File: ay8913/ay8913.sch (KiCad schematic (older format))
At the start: 5 parts, among them U2 74HCT138, U3 GAL16V8, U4 AY-3-8913, U5 XTAL_OSC_HALF_CAN, U6 74HC74

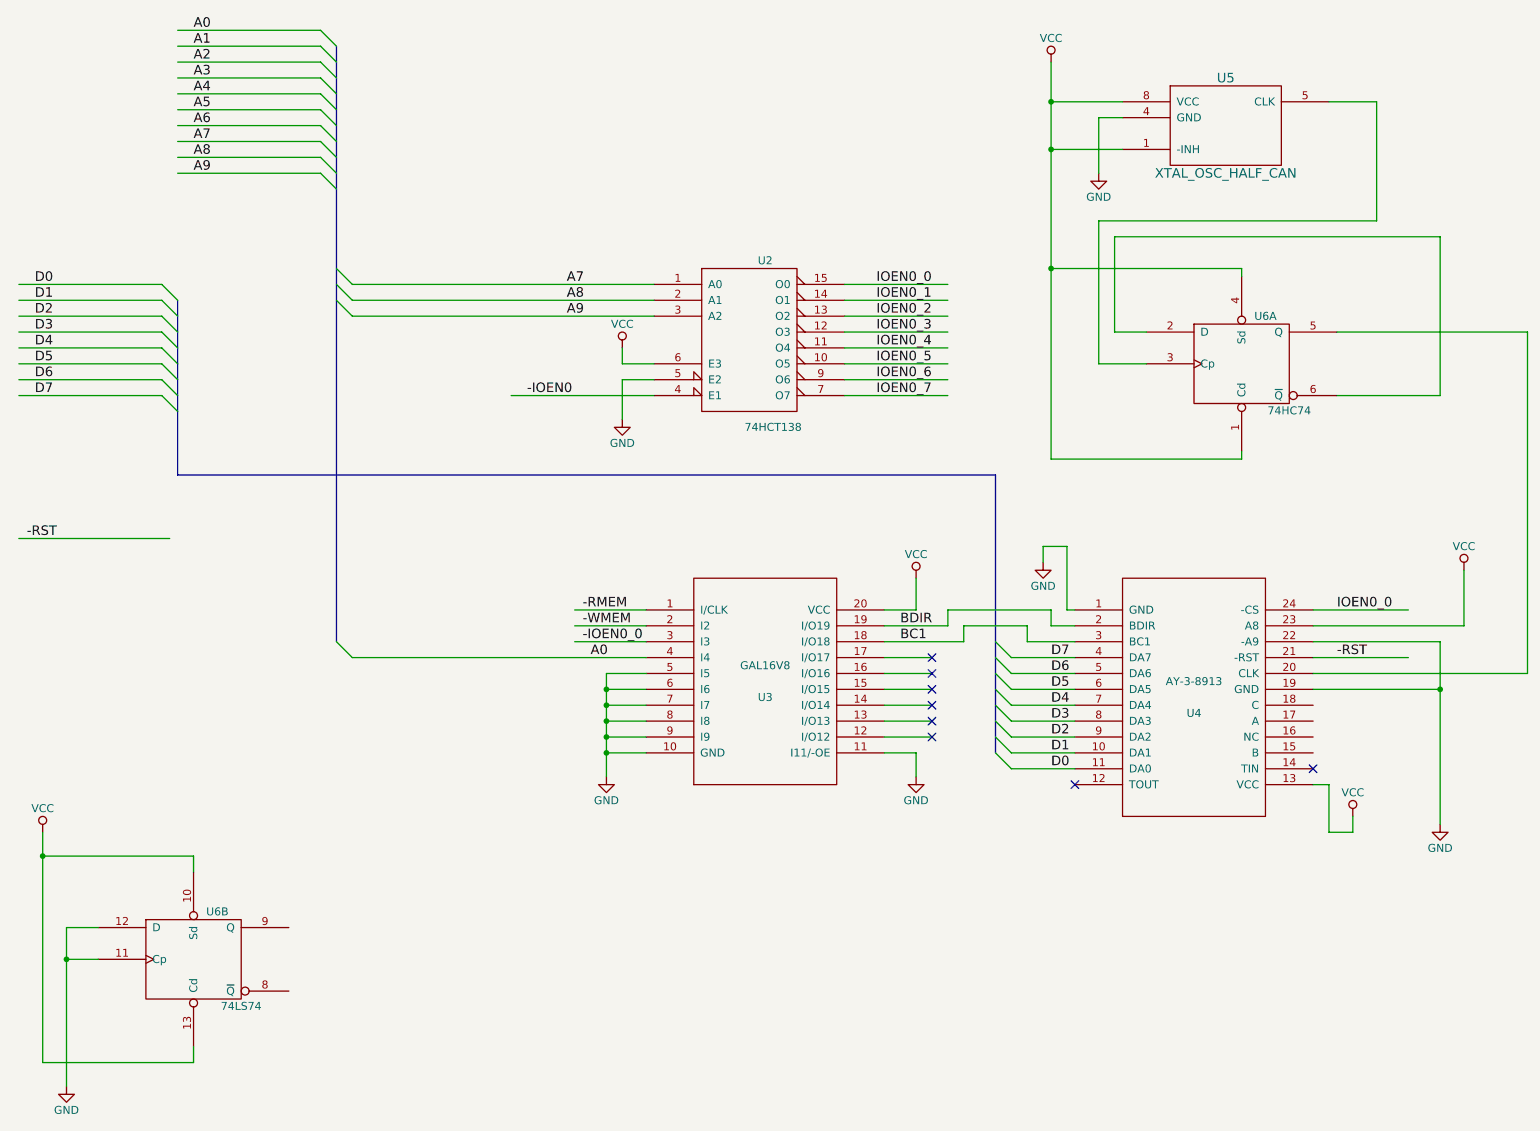
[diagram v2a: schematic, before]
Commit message: use GAL16V8 to divide the 4MHz to 2MHz
This works fine and eliminates the need for the 74HC74.
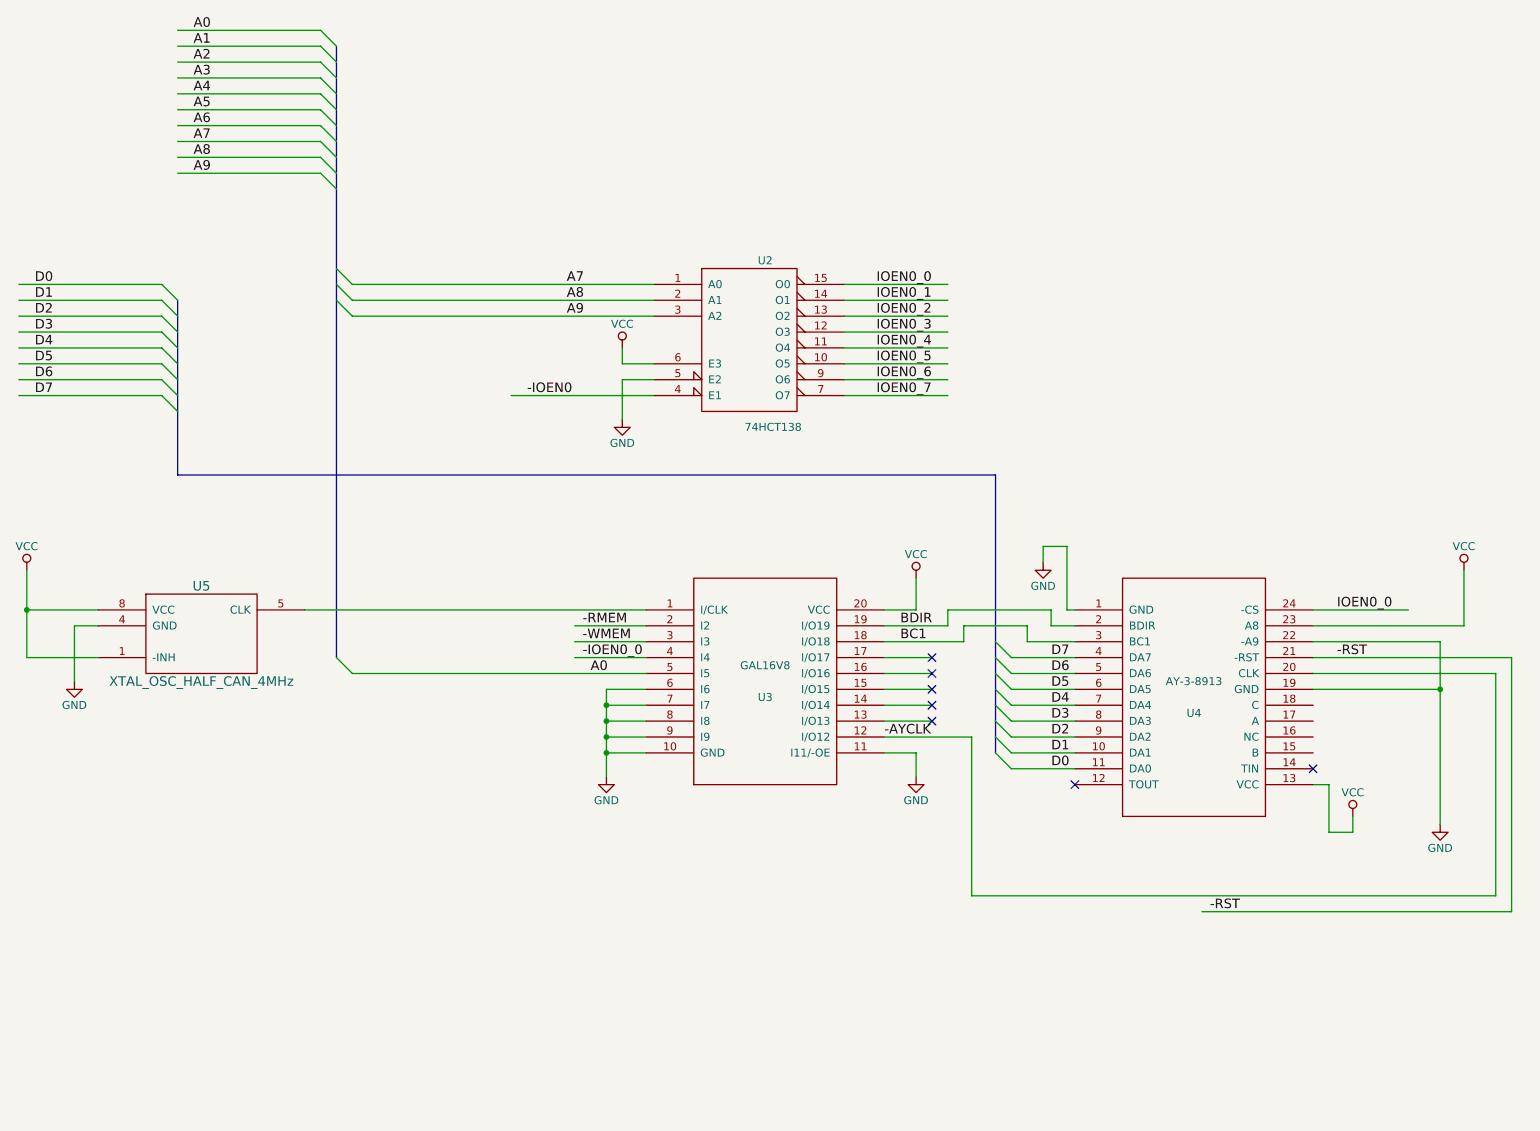
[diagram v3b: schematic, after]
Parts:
- removed U6: 74HC74, symbol 74LS74
- U5: value XTAL_OSC_HALF_CAN -> XTAL_OSC_HALF_CAN_4MHz
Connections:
- net labels added: -AYCLK
- wire segments 119 -> 99
- no-connect marks 8 -> 7
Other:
- moved on the sheet: U5
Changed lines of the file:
@@
 	1    0    0    -1
 $EndComp
-Text Label 4350 4350 0    60   ~ 0
+Text Label 4350 4450 0    60   ~ 0
 -RMEM
-Text Label 4350 4450 0    60   ~ 0
+Text Label 4350 4550 0    60   ~ 0
 -WMEM
-Text Label 4350 4550 0    60   ~ 0
+Text Label 4350 4650 0    60   ~ 0
 -IOEN0_0
-Text Label 4400 4650 0    60   ~ 0
+Text Label 4400 4750 0    60   ~ 0
 A0
 $Comp
@@
 NoConn ~ 6550 4950
 NoConn ~ 6550 5050
-NoConn ~ 6550 5150
 $Comp
 L GND #PWR7
@@
 	2700 1600 2800 1700
 Entry Wire Line
-	2800 4550 2900 4650
+	2800 4650 2900 4750
 Entry Wire Line
 	2800 2200 2900 2300
@@
 	8950 4350 9550 4350
 Wire Wire Line
-	4750 4350 4300 4350
-Wire Wire Line
 	4750 4450 4300 4450
 Wire Wire Line
 	4750 4550 4300 4550
 Wire Wire Line
-	2900 4650 4750 4650
+	4750 4650 4300 4650
+Wire Wire Line
+	2900 4750 4750 4750
 Wire Wire Line
 	4500 5250 4750 5250
 Wire Wire Line
-	4500 4750 4500 5400
+	4500 4850 4500 5400
 Wire Wire Line
 	6250 4350 6450 4350
@@
 	6250 5050 6550 5050
 Wire Wire Line
-	6250 5150 6550 5150
-Wire Wire Line
-	4750 4750 4500 4750
+	6250 5150 6800 5150
 Connection ~ 4500 5250
 Wire Wire Line
@@
 Wire Wire Line
 	4750 4850 4500 4850
-Connection ~ 4500 4850
 Wire Wire Line
 	6250 5250 6450 5250
@@
 	6450 5250 6450 5400
 Wire Bus Line
-	2800 800  2800 4550
+	2800 800  2800 4650
 Wire Bus Line
 	1800 2400 1800 3500
@@
 L XTAL_OSC_HALF_CAN U5
 U 1 1 5AB2F1FD
-P 8400 1300
-F 0 "U5" H 8400 1600 60  0000 C CNN
-F 1 "XTAL_OSC_HALF_CAN" H 8400 1000 60  0000 C CNN
-F 2 "" H 8400 1300 60  0000 C CNN
-F 3 "" H 8400 1300 60  0000 C CNN
-	1    8400 1300
-	1    0    0    -1
-$EndComp
-$Comp
-L 74LS74 U6
-U 1 1 5AB2F240
-P 8500 2800
-F 0 "U6" H 8650 3100 50  0000 C CNN
-F 1 "74HC74" H 8800 2505 50  0000 C CNN
-F 2 "" H 8500 2800 50  0001 C CNN
-F 3 "" H 8500 2800 50  0001 C CNN
-	1    8500 2800
-	1    0    0    -1
-$EndComp
-Wire Wire Line
-	7300 1450 7750 1450
-Wire Wire Line
-	7300 900  7300 3400
-Wire Wire Line
-	7750 1150 7300 1150
-Connection ~ 7300 1150
+P 1950 4500
+F 0 "U5" H 1950 4800 60  0000 C CNN
+F 1 "XTAL_OSC_HALF_CAN_4MHz" H 1950 4200 60  0000 C CNN
+F 2 "" H 1950 4500 60  0000 C CNN
+F 3 "" H 1950 4500 60  0000 C CNN
+	1    1950 4500
+	1    0    0    -1
+$EndComp
 $Comp
 L VCC #PWR9
 U 1 1 5AB2F373
-P 7300 900
-F 0 "#PWR9" H 7300 750 50  0001 C CNN
-F 1 "VCC" H 7300 1050 50  0000 C CNN
-F 2 "" H 7300 900 50  0001 C CNN
-F 3 "" H 7300 900 50  0001 C CNN
-	1    7300 900
-	1    0    0    -1
-$EndComp
-Wire Wire Line
-	7750 1250 7600 1250
-Wire Wire Line
-	7600 1250 7600 1600
+P 850 4100
+F 0 "#PWR9" H 850 3950 50  0001 C CNN
+F 1 "VCC" H 850 4250 50  0000 C CNN
+F 2 "" H 850 4100 50  0001 C CNN
+F 3 "" H 850 4100 50  0001 C CNN
+	1    850  4100
+	1    0    0    -1
+$EndComp
+Wire Wire Line
+	1300 4450 1150 4450
+Wire Wire Line
+	1150 4450 1150 4800
 $Comp
 L GND #PWR10
 U 1 1 5AB2F3FE
-P 7600 1600
-F 0 "#PWR10" H 7600 1350 50  0001 C CNN
-F 1 "GND" H 7600 1450 50  0000 C CNN
-F 2 "" H 7600 1600 50  0001 C CNN
-F 3 "" H 7600 1600 50  0001 C CNN
-	1    7600 1600
-	1    0    0    -1
-$EndComp
-Wire Wire Line
-	9050 1150 9350 1150
-Wire Wire Line
-	9350 1150 9350 1900
-Wire Wire Line
-	9350 1900 7600 1900
-Wire Wire Line
-	7600 1900 7600 2800
-Wire Wire Line
-	7600 2800 7900 2800
-Wire Wire Line
-	9100 3000 9750 3000
-Wire Wire Line
-	9750 3000 9750 2000
-Wire Wire Line
-	9750 2000 7700 2000
-Wire Wire Line
-	7700 2000 7700 2600
-Wire Wire Line
-	7700 2600 7900 2600
-Wire Wire Line
-	8500 2250 8500 2200
-Wire Wire Line
-	8500 2200 7300 2200
-Connection ~ 7300 1450
-Wire Wire Line
-	8500 3350 8500 3400
-Wire Wire Line
-	8500 3400 7300 3400
-Connection ~ 7300 2200
-Wire Wire Line
-	9100 2600 10300 2600
-Wire Wire Line
-	10300 2600 10300 4750
-Wire Wire Line
-	10300 4750 8950 4750
-$Comp
-L 74LS74 U6
-U 2 1 5AB2F827
-P 1900 6550
-F 0 "U6" H 2050 6850 50  0000 C CNN
-F 1 "74LS74" H 2200 6255 50  0000 C CNN
-F 2 "" H 1900 6550 50  0001 C CNN
-F 3 "" H 1900 6550 50  0001 C CNN
-	2    1900 6550
-	1    0    0    -1
-$EndComp
-Wire Wire Line
-	1900 6000 1900 5900
-Wire Wire Line
-	1900 5900 950  5900
-Wire Wire Line
-	950  5750 950  7200
-Wire Wire Line
-	1900 7100 1900 7200
-Wire Wire Line
-	1900 7200 950  7200
-Connection ~ 950  5900
-$Comp
-L VCC #PWR1
-U 1 1 5AB2F980
-P 950 5750
-F 0 "#PWR1" H 950 5600 50  0001 C CNN
-F 1 "VCC" H 950 5900 50  0000 C CNN
-F 2 "" H 950 5750 50  0001 C CNN
-F 3 "" H 950 5750 50  0001 C CNN
-	1    950  5750
-	1    0    0    -1
-$EndComp
-Wire Wire Line
-	1300 6350 1100 6350
-Wire Wire Line
-	1100 6350 1100 7350
-Wire Wire Line
-	1300 6550 1100 6550
-Connection ~ 1100 6550
-$Comp
-L GND #PWR2
-U 1 1 5AB2FAB4
-P 1100 7350
-F 0 "#PWR2" H 1100 7100 50  0001 C CNN
-F 1 "GND" H 1100 7200 50  0000 C CNN
-F 2 "" H 1100 7350 50  0001 C CNN
-F 3 "" H 1100 7350 50  0001 C CNN
-	1    1100 7350
-	1    0    0    -1
-$EndComp
-Wire Wire Line
-	800  3900 1750 3900
-Text Label 850  3900 0    60   ~ 0
+P 1150 4800
+F 0 "#PWR10" H 1150 4550 50  0001 C CNN
+F 1 "GND" H 1150 4650 50  0000 C CNN
+F 2 "" H 1150 4800 50  0001 C CNN
+F 3 "" H 1150 4800 50  0001 C CNN
+	1    1150 4800
+	1    0    0    -1
+$EndComp
+Wire Wire Line
+	8250 6250 10200 6250
+Text Label 8300 6250 0    60   ~ 0
 -RST
 Wire Wire Line
-	8950 4650 9550 4650
+	8950 4650 10200 4650
 Text Label 9100 4650 0    60   ~ 0
 -RST
+Wire Wire Line
+	850  4650 1300 4650
+Wire Wire Line
+	850  4100 850  4650
+Wire Wire Line
+	1300 4350 850  4350
+Connection ~ 850  4350
+Wire Wire Line
+	10200 4650 10200 6250
+Wire Wire Line
+	4750 4350 2600 4350
+Wire Wire Line
+	6800 5150 6800 6150
+Wire Wire Line
+	6800 6150 10100 6150
+Wire Wire Line
+	10100 6150 10100 4750
+Wire Wire Line
+	10100 4750 8950 4750
+Text Label 6250 5150 0    60   ~ 0
+-AYCLK
 $EndSCHEMATC
